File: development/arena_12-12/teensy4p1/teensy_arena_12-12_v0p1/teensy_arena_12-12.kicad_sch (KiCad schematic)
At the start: 0 parts

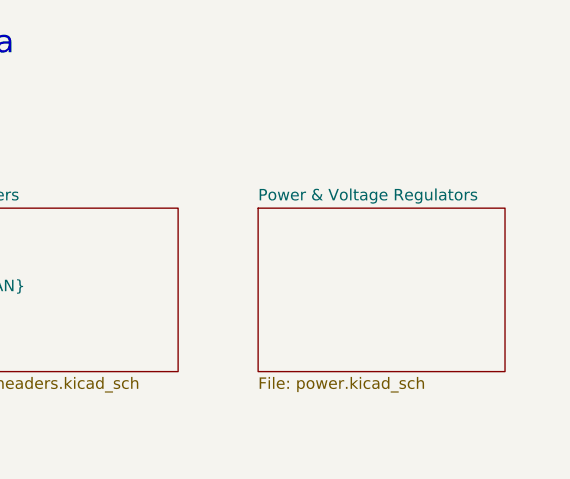
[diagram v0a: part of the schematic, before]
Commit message: Worked on routing of ni 12-12 arena with vreg.
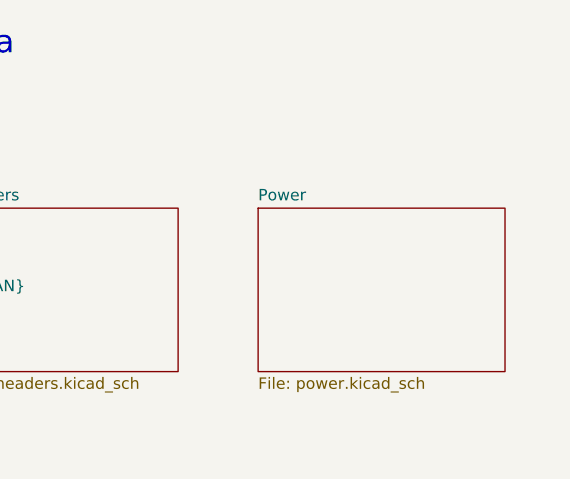
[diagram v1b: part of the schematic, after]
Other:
- sheet Power & Voltage Regulators renamed Power
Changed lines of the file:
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@@
     (stroke (width 0.1524) (type solid))
     (fill (color 0 0 0 0.0000))
-    (property "Sheetname" "Power & Voltage Regulators" (at 175.26 49.0724 0)
+    (property "Sheetname" "Power" (at 175.26 49.0724 0)
       (effects (font (size 1.27 1.27)) (justify left bottom))
     )
